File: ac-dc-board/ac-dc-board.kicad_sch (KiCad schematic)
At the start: 0 parts

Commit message: add componets
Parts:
- added F1: 03540101ZXGY, my_Fuse:03540101ZXGY, symbol my_Fuse:03540101ZXGY
- added J1: 6ESRM-P, my_Connector:6ESRM-P, symbol my_Connector:6ESRM-P
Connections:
- new net Earth: J1.3 (PE)
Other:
- added sheet ac-filter (ac-filter.kicad_sch)
- added sheet active-bridge (active-bridge.kicad_sch)

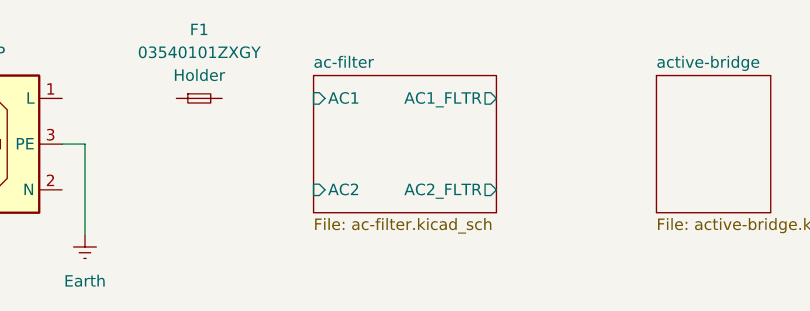
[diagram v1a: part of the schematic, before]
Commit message: modify lavel name
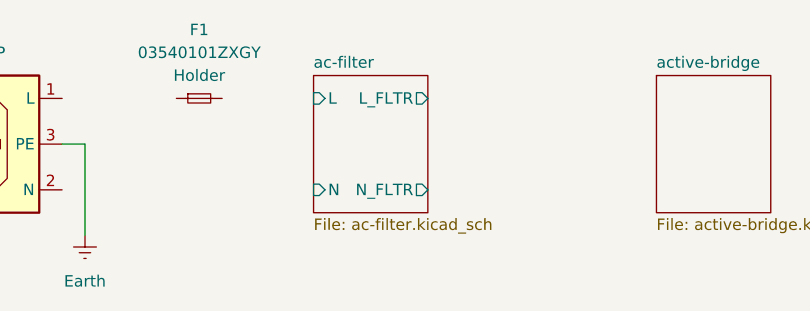
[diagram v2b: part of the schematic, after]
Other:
- sheet ac-filter ports: added L, L_FLTR, N, N_FLTR; removed AC1, AC1_FLTR, AC2, AC2_FLTR
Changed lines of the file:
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@@
 	(sheet
 		(at 76.2 43.18)
-		(size 20.32 15.24)
+		(size 12.7 15.24)
 		(exclude_from_sim no)
 		(in_bom yes)
@@
 			)
 		)
-		(pin "AC1" input
+		(pin "L" input
 			(at 76.2 45.72 180)
 			(effects
@@
 			)
 		)
-		(pin "AC1_FLTR" output
-			(at 96.52 45.72 0)
+		(pin "N_FLTR" output
+			(at 88.9 55.88 0)
 			(effects
 				(font
@@
 			)
 		)
-		(pin "AC2" input
+		(pin "L_FLTR" output
+			(at 88.9 45.72 0)
+			(effects
+				(font
+					(size 1.27 1.27)
+				)
+				(justify right)
+			)
+		)
+		(pin "N" input
 			(at 76.2 55.88 180)
 			(effects
@@
 			)
 		)
-		(pin "AC2_FLTR" output
-			(at 96.52 55.88 0)
-			(effects
-				(font
-					(size 1.27 1.27)
-				)
-				(justify right)
-			)
-		)

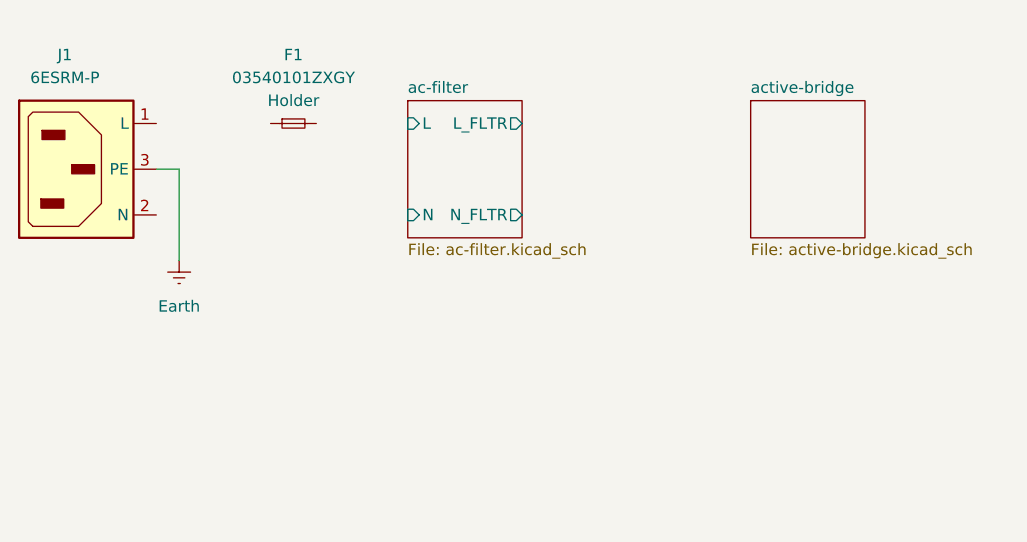
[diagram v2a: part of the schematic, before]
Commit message: add parts for protection
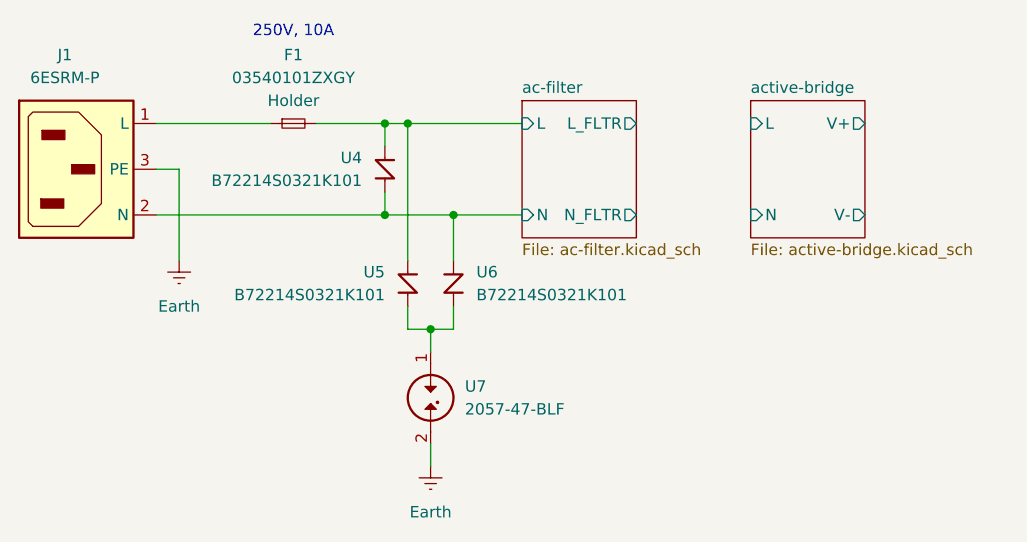
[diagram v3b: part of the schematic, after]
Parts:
- added U4, U5, U6: B72214S0321K101, my_Protection:B72214S0321K101, symbol my_Protection:B72214S0321K101
- added U7: 2057-47-BLF, my_Protection:2057-47-BLF, symbol my_Protection:2057-47-BLF
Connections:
- net Earth: now also U7.2
- net ac-filter/L: now also F1.2, U4.1, U5.1
- net ac-filter/N: now also J1.2 (N), U4.2, U6.1
- net at J1.1 (L): now also F1.1
- new net: U5.2, U6.2, U7.1
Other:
- sheet active-bridge ports: added L, N, V+, V-; removed none
- note added: "250V, 10A"

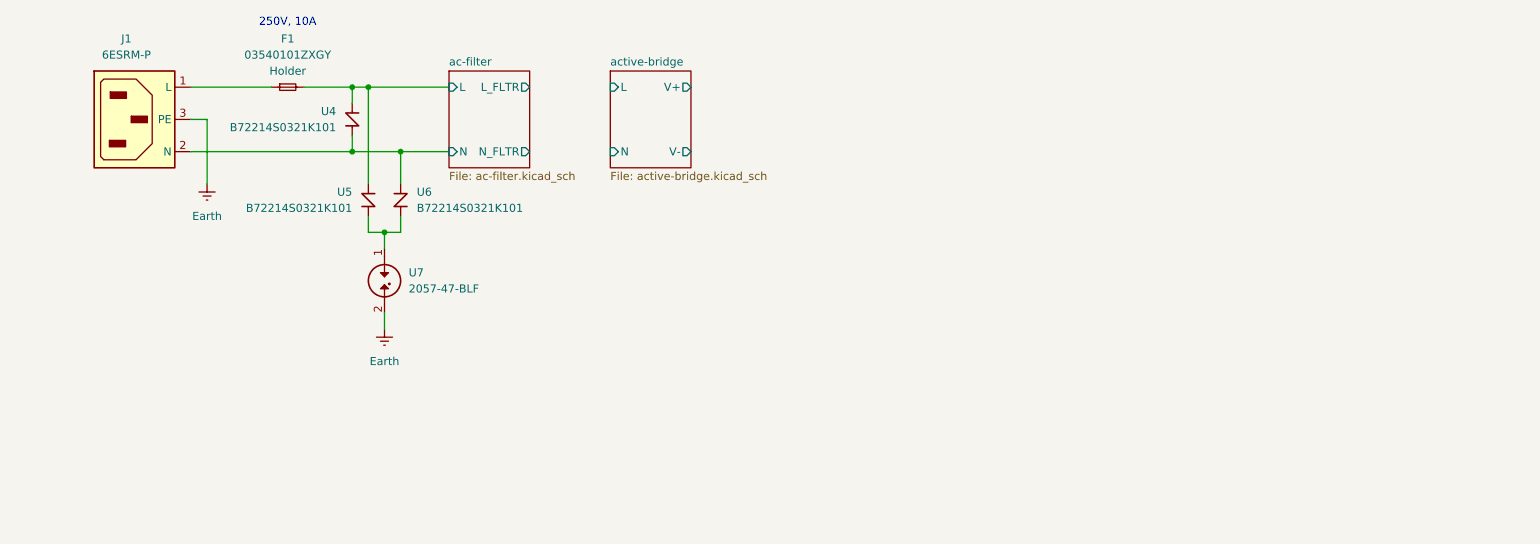
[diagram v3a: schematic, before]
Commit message: add components of pfc
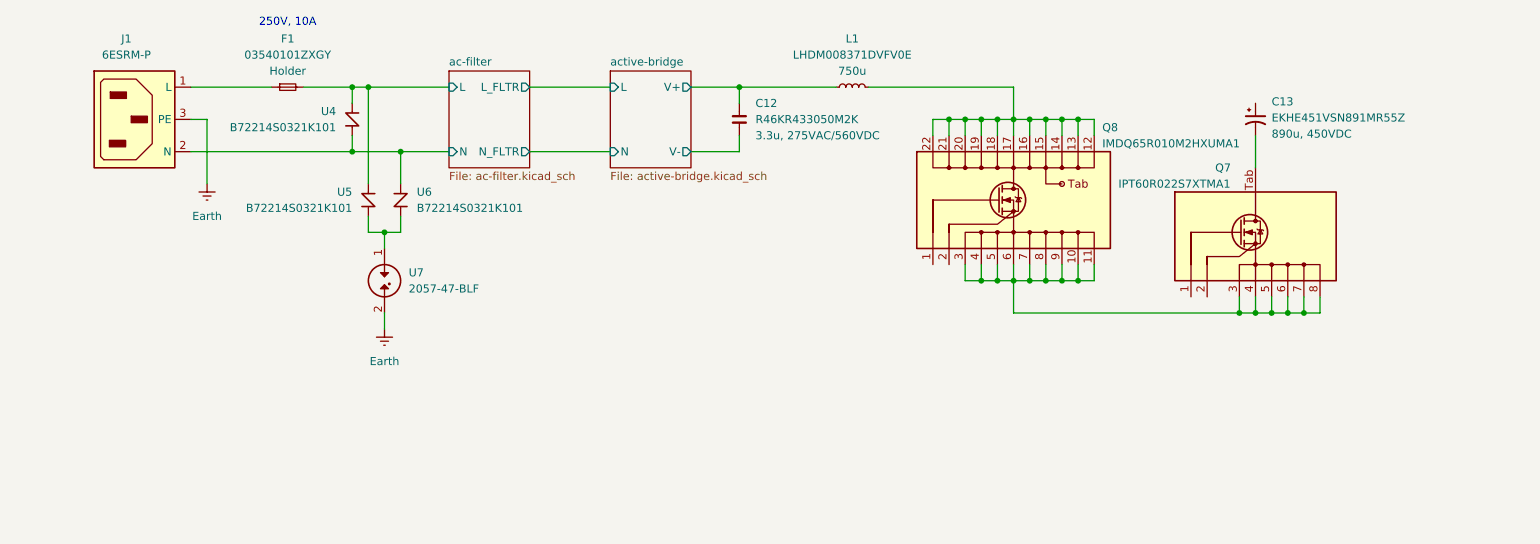
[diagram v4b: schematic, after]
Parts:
- added C12: R46KR433050M2K, my_Capacitor:R46KR433050M2K, symbol my_Capacitor:R46KR433050M2K
- added C13: EKHE451VSN891MR55Z, my_Capacitor:EKHE451VSN891MR55Z, symbol my_Capacitor:EKHE451VSN891MR55Z
- added L1: LHDM008371DVFV0E, my_Inductor:LHDM008371DVFV0E, symbol my_Inductor:LHDM008371DVFV0E
- added Q7: IPT60R022S7XTMA1, my_Transistor:IPT60R022S7XTMA1, symbol my_Transistor:IPT60R022S7XTMA1
- added Q8: IMDQ65R010M2HXUMA1, my_Transistor:IMDQ65R010M2HXUMA1, symbol my_Transistor:IMDQ65R010M2HXUMA1
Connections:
- net active-bridge/V+: now also C12.1, L1.1
- net active-bridge/V-: now also C12.2
- new net: L1.2, Q8.12 (Drain), Q8.13 (Drain), Q8.14 (Drain), Q8.15 (Drain), Q8.16 (Drain), Q8.17 (Drain), Q8.18 (Drain), Q8.19 (Drain), Q8.20 (Drain), Q8.21 (Drain), Q8.22 (Drain)
- new net: Q7.3 (Source), Q7.4 (Source), Q7.5 (Source), Q7.6 (Source), Q7.7 (Source), Q7.8 (Source), Q8.10 (Source), Q8.11 (Source), Q8.3 (Source), Q8.4 (Source), Q8.5 (Source), Q8.6 (Source), Q8.7 (Source), Q8.8 (Source), Q8.9 (Source)
- new net: C13.2, Q7.Tab (Drain)

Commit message: add pfc diode, precharge ntc
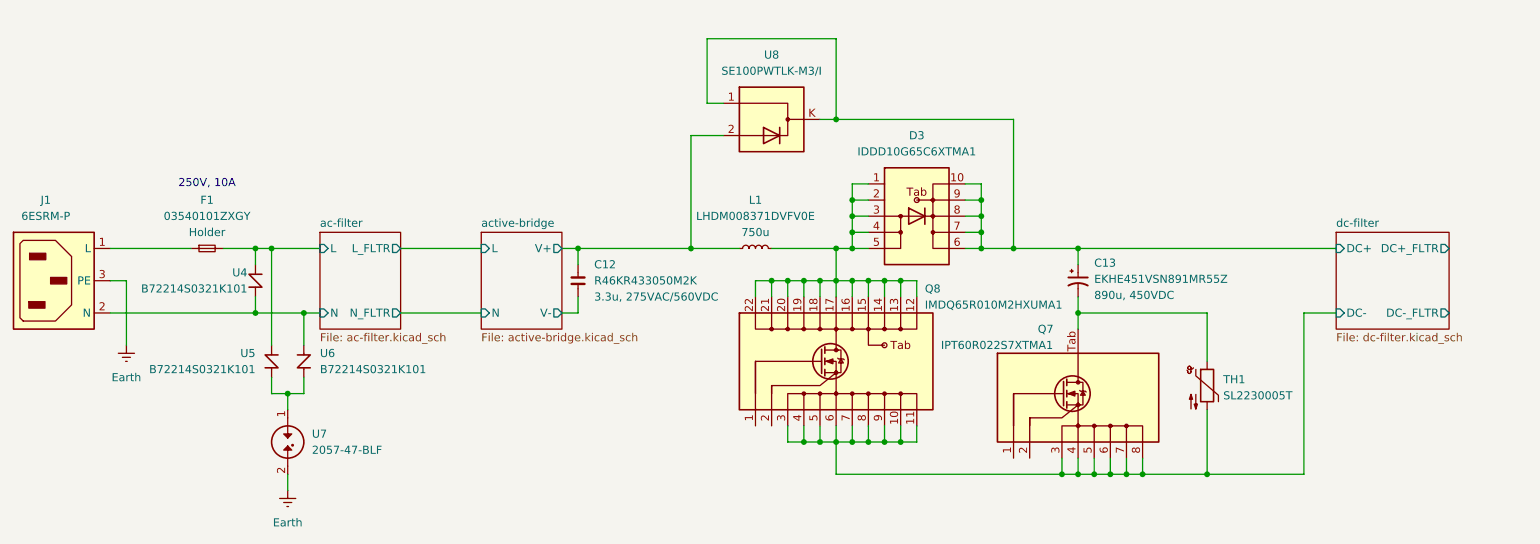
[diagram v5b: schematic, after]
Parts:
- added D3: IDDD10G65C6XTMA1, my_Diode:IDDD10G65C6XTMA1, symbol my_Diode:IDDD10G65C6XTMA1
- added TH1: SL2230005T, my_Protection:SL2230005T, symbol my_Protection:SL2230005T
- added U8: SE100PWTLK-M3/I, my_Diode:SE100PWTLK-M3_I, symbol my_Diode:SE100PWTLK-M3/I
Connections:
- net active-bridge/V+: now also U8.2
- net at L1.2, Q8.12 (Drain), Q8.13 (Drain)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: now also D3.1 (n.c.), D3.2 (n.c.), D3.3 (Anode), D3.4 (Anode), D3.5 (Anode)
- net dc-filter/DC-: now reaches Q7.3 (Source), Q7.4 (Source), Q7.5 (Source), Q7.6 (Source), Q7.7 (Source), Q7.8 (Source), Q8.10 (Source), Q8.11 (Source), Q8.3 (Source), Q8.4 (Source), Q8.5 (Source), Q8.6 (Source), Q8.7 (Source), Q8.8 (Source), Q8.9 (Source)
- net dc-filter/DC-: now also TH1.2
- net at C13.2, Q7.Tab (Drain): now also TH1.1
- net dc-filter/DC+: now reaches C13.1
- net dc-filter/DC+: now also D3.10 (Cathode), D3.6 (Cathode), D3.7 (Cathode), D3.8 (Cathode), D3.9 (Cathode), U8.1, U8.K
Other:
- added sheet dc-filter (dc-filter.kicad_sch)
- moved on the sheet: C12, C13, F1, J1, L1, Q7, Q8, U4, U5, U6, U7
